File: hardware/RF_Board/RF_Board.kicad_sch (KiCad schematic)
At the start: 79 parts, among them J1 Conn_Coaxial, J2 Conn_01x07_Male, J3 Conn_Coaxial, J4 Conn_01x07_Male, J5 Conn_01x06_Female, J6 Conn_01x06_Female, J7 Conn_01x06_Female, U1 MSP430FR2355TPT, U10 QPL9096, U11 QPL9096, U12 74AHC04, U13 RFM95PW, U2 MSP430FR2355TPT, U3 CC2500, U4 HMC574, U5 HMC574, U6 YAT-5A+, U7 SKY65900-11, U8 LFCN-2750+, U9 DEA202450BT-1213C1, Y1 Crystal_GND24, Y2 Crystal, Y3 Crystal

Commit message: more work
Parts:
- added J9: LD15S33E4GX00LF, LD15S33E4GX00LF, symbol RF_Board_Symbols:LD15S33E4GX00LF
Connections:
- net +3.3V: now also J9.9
- net +5V: now also J7.3 (Pin_3), J7.4 (Pin_4), J9.15
- net CC2500_UART_RX: now also J9.7
- net CC2500_UART_TX: now also J9.8
- net GND: now also J7.5 (Pin_5), J7.6 (Pin_6), J9.12, J9.MH1, J9.MH2
- net RFM_CSN: now also J5.2 (Pin_2)
- net RFM_DIO0: now also J6.4 (Pin_4), U1.30 (P2.0/TB1.1/COMP0.O)
- net RFM_DIO1: now also J6.3 (Pin_3)
- net RFM_DIO2: now also J6.2 (Pin_2)
- net RFM_DIO3: now also J6.6 (Pin_6)
- net RFM_DIO4: now also J6.5 (Pin_5)
- net RFM_DIO5: now also J6.1 (Pin_1)
- net RFM_MISO: now also J5.5 (Pin_5)
- net RFM_MOSI: now also J5.4 (Pin_4)
- net RFM_RST: now also J5.1 (Pin_1), U1.28 (P2.2/TB1CLK)
- net RFM_SCLK: now also J5.3 (Pin_3)
- net RFM_UART_RX: now also J9.3
- net RFM_UART_TX: now also J9.4
- net RFM_3V3_OUT: now reaches U13.1 (3V3_OUT)
- net RFM_3V3_OUT: now also J5.6 (Pin_6)

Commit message: add more RF board footprints/work on layout
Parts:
- added C46: 1uF, RF_Board_Footprints:C_0603_1608Metric, symbol RF_Board_Symbols:C
- added C47: 100nF, RF_Board_Footprints:C_0603_1608Metric, symbol RF_Board_Symbols:C
- added D1, D2: D_Zener, symbol RF_Board_Symbols:D_Zener
- added D3, D4: LED, RF_Board_Footprints:LED_0603_1608Metric, symbol RF_Board_Symbols:LED
- added F1, F2: Polyfuse, symbol RF_Board_Symbols:Polyfuse
- added R10, R8, R9: 10k, symbol RF_Board_Symbols:R_US
- added R11: 10k, RF_Board_Footprints:R_0603_1608Metric, symbol RF_Board_Symbols:R_US
- added R6: 480, RF_Board_Footprints:R_0603_1608Metric, symbol RF_Board_Symbols:R_US
- added R7: 330, RF_Board_Footprints:R_0603_1608Metric, symbol RF_Board_Symbols:R_US
- C25, C36, C38, C43: footprint (none) -> RF_Board_Footprints:C_0603_1608Metric
- C37, C39, C45: footprint (none) -> RF_Board_Footprints:C_1206_3216Metric
- J1, J3: footprint (none) -> RF_Board_Footprints:SMA_Amphenol_901-144_Vertical
- U1, U2: footprint QFP50P900X900X160-48N -> RF_Board_Footprints:QFP50P900X900X160-48N
- U10, U11: footprint (none) -> RF_Board_Footprints:QPL9504TR7
- U3: footprint Package_DFN_QFN:Texas_S-PVQFN-N20_EP2.4x2.4mm -> RF_Board_Footprints:Texas_S-PVQFN-N20_EP2.4x2.4mm
- U4, U5: footprint (none) -> RF_Board_Footprints:HMC574AMS8E
- U6: footprint (none) -> RF_Board_Footprints:YAT-1A&plus_
- U7: footprint (none) -> RF_Board_Footprints:QFN-16-1EP_4x4mm_P0.65mm_EP2.5x2.5mm
- U8: footprint (none) -> RF_Board_Footprints:LFCN-2500&plus_
- U9: footprint (none) -> RF_Board_Footprints:DEA202450BT-1213C1
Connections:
- net +3.3V: now also C25.1, C46.2, C47.1, D2.1 (K), D4.1 (K), F1.2, R10.1, R8.1, R9.1; no longer J9.9
- net +5V: now also D1.1 (K), D3.1 (K), F2.2; no longer C25.1, J9.15
- net GND: now also C46.1, C47.2, D1.2 (A), D2.2 (A), R11.2, R6.2, R7.2
- net LNA_BP_A: now also U2.46 (P3.1/OA2O), R9.2
- net LNA_BP_B: now also U2.45 (P3.2/OA2-), R10.2
- net LNA_SD: now also U2.44 (P3.3/OA2+), R8.2
- net PA_EN: now also U2.38 (P3.4/SMCLK)
- net PA_VDET: now also U2.33 (P1.5/UCA0CLK/TMS/OA1O/A5)
- net RFM_DIO1: now also U1.29 (P2.1/TB1.2/COMP1.O)
- net RFM_DIO2: now also U1.28 (P2.2/TB1CLK)
- net RFM_DIO3: now also U1.27 (P2.3/TB1TRG)
- net RFM_DIO4: now also U1.11 (P2.4/COMP1.1)
- net RFM_DIO5: now also U1.10 (P2.5/COMP1.0)
- net RFM_RST: now also U1.34 (P1.4/UCA0STE/TCK/A4); no longer U1.28 (P2.2/TB1CLK)
- net SBAND_TX_RX: now also U2.37 (P3.5/OA3O), R11.1
- net CC2500_RX_EMPTY: now reaches U2.1 (P1.2/UCB0SIMO/UCB0SDA/TB0TRG/OA0-/A2/VEREF)
- net CC2500_RX_EMPTY: now also J9.5
- net CC2500_TX_OVERFLOW: now reaches U2.2 (P1.1/UCB0CLK/ACLK/OA0O/COMP0.1/A1)
- net CC2500_TX_OVERFLOW: now also J9.14
- net CC2500_RX_OVERFLOW: now reaches U2.3 (P1.0/UCB0STE/SMCLK/COMP0.0/A0/VEREF+)
- net CC2500_RX_OVERFLOW: now also J9.13
- net CC2500_TX_EMPTY: now reaches U2.48 (P1.3/UCB0SOMI/UCB0SCL/OA0+/A3)
- net CC2500_TX_EMPTY: now also J9.6
- net RFM_RX_EMPTY: now reaches U1.1 (P1.2/UCB0SIMO/UCB0SDA/TB0TRG/OA0-/A2/VEREF)
- net RFM_RX_EMPTY: now also J9.1
- net RFM_TX_OVERFLOW: now reaches U1.2 (P1.1/UCB0CLK/ACLK/OA0O/COMP0.1/A1)
- net RFM_TX_OVERFLOW: now also J9.11
- net RFM_RX_OVERFLOW: now reaches U1.3 (P1.0/UCB0STE/SMCLK/COMP0.0/A0/VEREF+)
- net RFM_RX_OVERFLOW: now also J9.10
- net RFM_TX_EMPTY: now reaches U1.48 (P1.3/UCB0SOMI/UCB0SCL/OA0+/A3)
- net RFM_TX_EMPTY: now also J9.2
- new net: D3.2 (A), R6.1
- new net: D4.2 (A), R7.1
- new net: F1.1, J9.9
- new net: F2.1, J9.15
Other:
- note added: "Power + I/O"
- note added: "S-Band"
- note added: "UHF"
- title: (none) -> R'SAT RF Board
- moved on the sheet: C1, C10, C11, C12, C13, C14, C15, C16, C17, C18, C19, C2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

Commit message: add power management to RF board + more PCB work
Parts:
- removed D1, D2: D_Zener, symbol RF_Board_Symbols:D_Zener
- removed F1, F2: Polyfuse, symbol RF_Board_Symbols:Polyfuse
- removed U12: 74AHC04, symbol RF_Board_Symbols:74AHC04
- added C48, C51: 100nF, RF_Board_Footprints:C_0603_1608Metric, symbol RF_Board_Symbols:C
- added C49, C52: 3.3nF, RF_Board_Footprints:C_0603_1608Metric, symbol RF_Board_Symbols:C
- added C50, C53: 1uF, RF_Board_Footprints:C_0805_2012Metric, symbol RF_Board_Symbols:C
- added D1, D7: D_TVS, RF_Board_Footprints:D_SMB_Handsoldering, symbol RF_Board_Symbols:D_TVS
- added D2, D8: D_Schottky, RF_Board_Footprints:D_SMB_Handsoldering, symbol Device:D_Schottky
- added D5, D6: LED, RF_Board_Footprints:LED_0603_1608Metric, symbol RF_Board_Symbols:LED
- added H1, H2, H3, H4: MountingHole_Pad, RF_Board_Footprints:MountingHole_4.3mm_M4_Pad_Via, symbol RF_Board_Symbols:MountingHole_Pad
- added Q1, Q2: 2N7002, RF_Board_Footprints:SOT-23-3, symbol RF_Board_Symbols:2N7002
- added R12, R13, R14, R15: 0, RF_Board_Footprints:R_0603_1608Metric, symbol RF_Board_Symbols:R_US
- added R16, R17: 330, RF_Board_Footprints:R_0603_1608Metric, symbol RF_Board_Symbols:R_US
- added R18: 100k, RF_Board_Footprints:R_0603_1608Metric, symbol RF_Board_Symbols:R_US
- added R19: 50k, RF_Board_Footprints:R_0603_1608Metric, symbol RF_Board_Symbols:R_US
- added R20: 3.3k, RF_Board_Footprints:R_0603_1608Metric, symbol RF_Board_Symbols:R_US
- added R21: 150k, RF_Board_Footprints:R_0603_1608Metric, symbol RF_Board_Symbols:R_US
- added R22: 39k, RF_Board_Footprints:R_0603_1608Metric, symbol RF_Board_Symbols:R_US
- added R23: 820, RF_Board_Footprints:R_0603_1608Metric, symbol RF_Board_Symbols:R_US
- added U12: 74HC04, RF_Board_Footprints:SOIC-14_3.9x8.7mm_P1.27mm, symbol RF_Board_Symbols:74HC04_ALT
- added U14, U15: TPS259573DSGR, RF_Board_Footprints:TPS259573DSGR, symbol RF_Board_Symbols:TPS259573DSGR
- C1, C16, C17, C2, C20, C21, C22, C24, C27, C28, C29, C3, C30, C31, C32, C35, C4, C5, C6, C9: footprint (none) -> RF_Board_Footprints:C_0402_1005Metric
- C10, C7: footprint (none) -> RF_Board_Footprints:C_0805_2012Metric
- C11, C12, C13, C14, C15, C19, C23, C26, C33, C34, C40, C41, C42, C44, C8, R5: footprint (none) -> RF_Board_Footprints:C_0603_1608Metric
- C18: footprint (none) -> RF_Board_Footprints:C_1206_3216Metric
- C46: footprint RF_Board_Footprints:C_0603_1608Metric -> RF_Board_Footprints:C_0805_2012Metric
- J2, J4: footprint (none) -> RF_Board_Footprints:PinHeader_1x07_P2.54mm_Vertical
- J5, J6, J7: footprint (none) -> RF_Board_Footprints:PinHeader_1x06_P2.54mm_Vertical
- J9: footprint LD15S33E4GX00LF -> RF_Board_Footprints:LD15S33E4GX00LF
- L3, L4, L5, L6: footprint (none) -> RF_Board_Footprints:L_0402_1005Metric
- R1, R10, R2, R3, R4, R8, R9: footprint (none) -> RF_Board_Footprints:R_0603_1608Metric
- Y1: footprint (none) -> RF_Board_Footprints:Crystal_SMD_3225-4Pin_3.2x2.5mm
- Y2: footprint (none) -> RF_Board_Footprints:ECS-.327-12.5-34B-TR
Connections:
- net +3.3V: now also C50.2, D2.1 (K), D5.1 (K), D6.1 (K), U12.14 (VCC), U14.5 (OUT)
- net +5V: now also C53.2, D8.1 (K), U15.5 (OUT)
- net CC2500_MOSI: now also Q1.1 (G)
- net GND: now also C48.2, C49.2, C50.1, C51.2, C52.2, C53.1, D1.2 (A2), D2.2 (A), D7.2 (A2), D8.2 (A), Q1.2 (S), Q2.2 (S), R12.2, R13.2, R14.2, R15.2, R19.2, R20.2, R22.2, R23.2, U12.7 (GND), U14.8 (GND), U14.9 (GND), U15.8 (GND), U15.9 (GND)
- net RFM_MOSI: now also Q2.1 (G)
- net SBAND_TX_RX: now also U12.1 (A1), U12.11 (A5)
- net SW1_A: now also U12.8 (Y4)
- net SW1_B: now also U12.10 (Y5), U12.9 (A4)
- net SW2_A: now also U12.6 (Y3)
- net SW2_B: now also U12.4 (Y2), U12.5 (A3)
- net 3V3_IN: now reaches J9.9
- net 3V3_IN: now also C48.1, D1.1 (A1), R18.1, U14.3 (IN), U14.4 (IN)
- net 5V0_IN: now reaches J9.15
- net 5V0_IN: now also C51.1, D7.1 (A1), R21.1, U15.3 (IN), U15.4 (IN)
- new net: D5.2 (A), R16.1
- new net: Q1.3 (D), R16.2
- new net: C49.1, U14.1 (DV_DT)
- new net: R21.2, R22.1, U15.2 (EN_UVLO)
- new net: R18.2, R19.1, U14.2 (EN_UVLO)
- new net: R20.1, U14.7 (ILM)
- new net: H2.1, R13.1
- new net: H3.1, R14.1
- new net: Q2.3 (D), R17.2
- new net: H1.1, R12.1
- new net: D6.2 (A), R17.1
- new net: C52.1, U15.1 (DV_DT)
- new net: R23.1, U15.7 (ILM)
- new net: H4.1, R15.1
- new net: U12.2 (Y1), U12.3 (A2)
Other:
- note added: "3V3 Rail: Shutdown voltage = 3.6V Shutdown current = 0.65A"
- note added: "5V0 Rail: Shutdown voltage = 5.7V Shutdown current = 2.5A"
- note added: "Consult NASA-HDBK-4001 for spacecraft grounding architecture guidelines"
- note added: "EN cutoff voltage = 1.2V"
- note added: "Rilm = 2000/(I - 0.04)"
- moved on the sheet: C25, D3, D4, J9, R11, R6, R7

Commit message: start RF Board layout
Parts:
- added R24, R25, R26, R27, R28, R29: 0, RF_Board_Footprints:R_0603_1608Metric, symbol RF_Board_Symbols:R_US
- L1, L2: value L -> 18nH; footprint (none) -> RF_Board_Footprints:L_0603_1608Metric
- Y3: footprint (none) -> RF_Board_Footprints:ECS-.327-12.5-34B-TR
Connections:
- net CC2500_MISO: now also R29.2
- net CC2500_MOSI: now also R28.2
- net CC2500_SCLK: now also R27.2
- net RFM_CSN: now also R26.1
- net RFM_DIO0: now also R24.1
- net RFM_MISO: now also R29.1
- net RFM_MOSI: now also R28.1
- net RFM_RST: now also R25.1
- net RFM_SCLK: now also R27.1
- net RFM_AUX_DIO0: now reaches U2.11 (P2.4/COMP1.1)
- net RFM_AUX_DIO0: now also R24.2
- net RFM_AUX_RST: now reaches U2.35 (P3.7/OA3+)
- net RFM_AUX_RST: now also R25.2
- net RFM_AUX_CSN: now reaches U2.36 (P3.6/OA3-)
- net RFM_AUX_CSN: now also R26.2

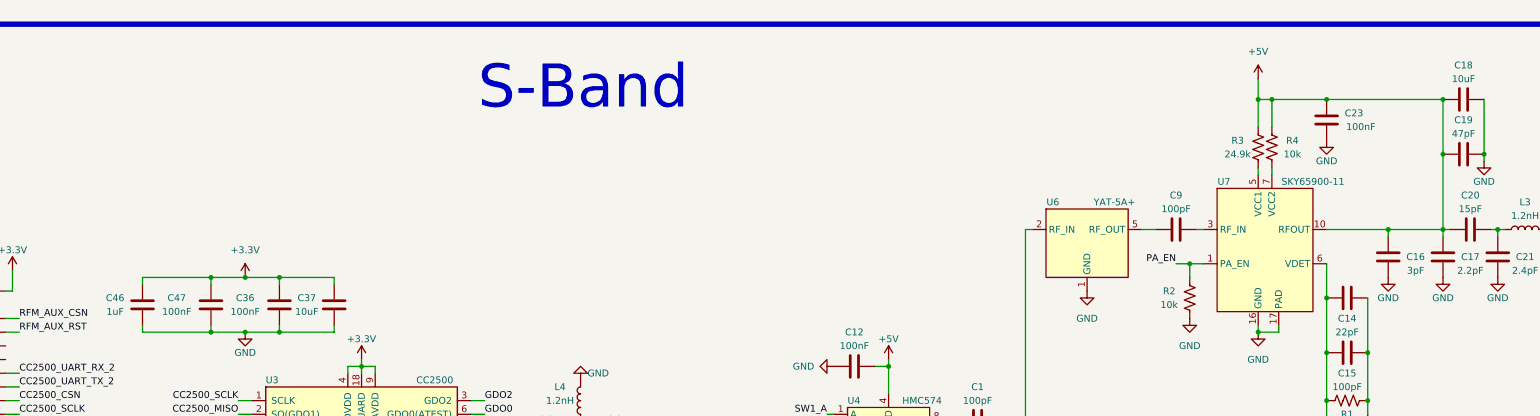
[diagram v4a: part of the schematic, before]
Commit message: RF board first draft placement
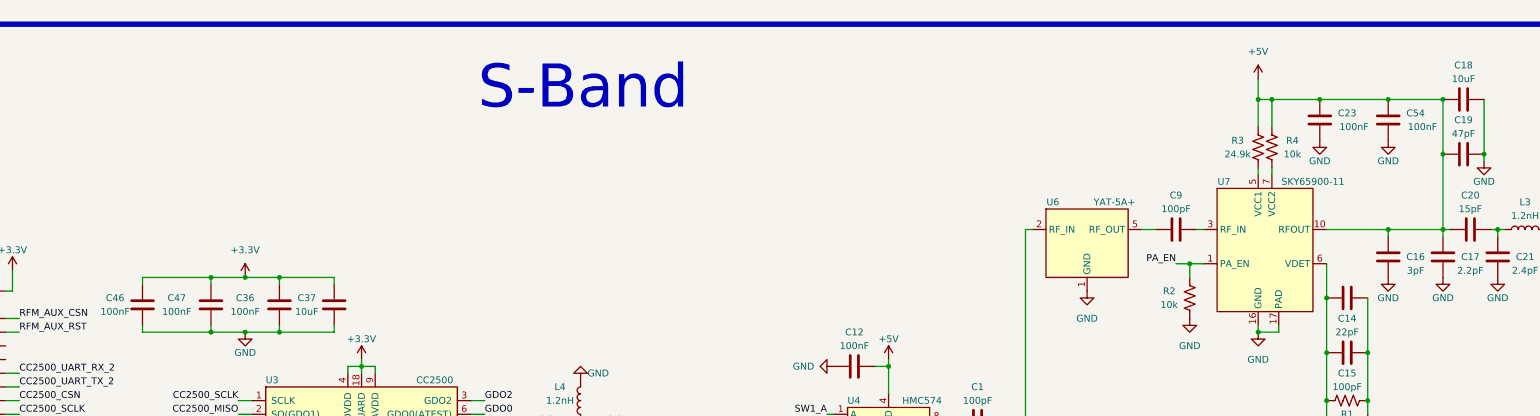
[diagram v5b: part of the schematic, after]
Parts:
- added C54: 100nF, RF_Board_Footprints:C_0603_1608Metric, symbol RF_Board_Symbols:C
- C46: value 1uF -> 100nF; footprint RF_Board_Footprints:C_0805_2012Metric -> RF_Board_Footprints:C_0603_1608Metric
- R18, R19, R20, R21, R22, R23: footprint RF_Board_Footprints:R_0603_1608Metric -> RF_Board_Footprints:R_0402_1005Metric
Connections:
- net +5V: now also C54.1
- net GND: now also C54.2
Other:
- moved on the sheet: C23
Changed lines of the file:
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@@
   (junction (at 457.2 219.71) (diameter 0) (color 0 0 0 0)
   )
+  (junction (at 447.04 195.58) (diameter 0) (color 0 0 0 0)
+  )
   (junction (at 313.69 262.89) (diameter 0) (color 0 0 0 0)
   )
@@
   (junction (at 425.45 195.58) (diameter 0) (color 0 0 0 0)
   )
-  (junction (at 435.61 195.58) (diameter 0) (color 0 0 0 0)
-  )
   (junction (at 234.95 228.6) (diameter 0) (color 0 0 0 0)
   )
   (junction (at 422.91 238.76) (diameter 0) (color 0 0 0 0)
   )
+  (junction (at 434.34 195.58) (diameter 0) (color 0 0 0 0)
+  )
   (wire (pts (xy 41.91 102.87) (xy 44.45 102.87))
     (stroke (width 0) (type default) (color 0 0 0 0))
@@
     (stroke (width 0) (type default) (color 0 0 0 0))
   )
+  (wire (pts (xy 434.34 195.58) (xy 447.04 195.58))
+    (stroke (width 0) (type default) (color 0 0 0 0))
+  )
   (wire (pts (xy 110.49 57.15) (xy 110.49 58.42))
     (stroke (width 0) (type default) (color 0 0 0 0))
@@
     (stroke (width 0) (type default) (color 0 0 0 0))
   )
+  (wire (pts (xy 447.04 195.58) (xy 457.2 195.58))
+    (stroke (width 0) (type default) (color 0 0 0 0))
+  )
   (wire (pts (xy 283.21 269.24) (xy 287.02 269.24))
     (stroke (width 0) (type default) (color 0 0 0 0))
@@
     (stroke (width 0) (type default) (color 0 0 0 0))
   )
-  (wire (pts (xy 435.61 195.58) (xy 457.2 195.58))
-    (stroke (width 0) (type default) (color 0 0 0 0))
-  )
   (wire (pts (xy 186.69 95.25) (xy 189.23 95.25))
     (stroke (width 0) (type default) (color 0 0 0 0))
@@
     (stroke (width 0) (type default) (color 0 0 0 0))
   )
-  (wire (pts (xy 425.45 195.58) (xy 435.61 195.58))
+  (wire (pts (xy 425.45 195.58) (xy 434.34 195.58))
     (stroke (width 0) (type default) (color 0 0 0 0))
   )
@@
       (effects (font (size 1.27 1.27)) (justify left))
     )
-    (property "Footprint" "RF_Board_Footprints:R_0603_1608Metric" (id 2) (at 488.696 103.124 90)
+    (property "Footprint" "RF_Board_Footprints:R_0402_1005Metric" (id 2) (at 488.696 103.124 90)
       (effects (font (size 1.27 1.27)) hide)
     )
@@
     (pin "1")
   )
+  (symbol (lib_id "power:GND") (at 447.04 203.2 0) (unit 1)
+    (in_bom yes) (on_board yes)
+    (property "Reference" "#PWR0103" (id 0) (at 447.04 209.55 0)
+      (effects (font (size 1.27 1.27)) hide)
+    )
+    (property "Value" "GND" (id 1) (at 447.04 207.01 0))
+    (property "Footprint" "" (id 2) (at 447.04 203.2 0)
+      (effects (font (size 1.27 1.27)) hide)
+    )
+    (property "Datasheet" "" (id 3) (at 447.04 203.2 0)
+      (effects (font (size 1.27 1.27)) hide)
+    )
+    (pin "1")
+  )
   (symbol (lib_id "RF_Board_Symbols:R_US") (at 487.68 59.69 0) (unit 1)
     (in_bom yes) (on_board yes) (fields_autoplaced)
@@
       (effects (font (size 1.27 1.27)) (justify left))
     )
-    (property "Footprint" "RF_Board_Footprints:R_0603_1608Metric" (id 2) (at 488.696 59.944 90)
+    (property "Footprint" "RF_Board_Footprints:R_0402_1005Metric" (id 2) (at 488.696 59.944 90)
       (effects (font (size 1.27 1.27)) hide)
     )
@@
     (pin "7")
   )
-  (symbol (lib_id "RF_Board_Symbols:C") (at 435.61 199.39 0) (unit 1)
+  (symbol (lib_id "RF_Board_Symbols:C") (at 434.34 199.39 0) (unit 1)
     (in_bom yes) (on_board yes)
-    (property "Reference" "C23" (id 0) (at 440.69 198.12 0))
-    (property "Value" "100nF" (id 1) (at 441.96 200.66 0))
-    (property "Footprint" "RF_Board_Footprints:C_0603_1608Metric" (id 2) (at 436.5752 203.2 0)
+    (property "Reference" "C23" (id 0) (at 439.42 198.12 0))
+    (property "Value" "100nF" (id 1) (at 440.69 200.66 0))
+    (property "Footprint" "RF_Board_Footprints:C_0603_1608Metric" (id 2) (at 435.3052 203.2 0)
       (effects (font (size 1.27 1.27)) hide)
     )
-    (property "Datasheet" "~" (id 3) (at 435.61 199.39 0)
+    (property "Datasheet" "~" (id 3) (at 434.34 199.39 0)
       (effects (font (size 1.27 1.27)) hide)
     )
@@
       (effects (font (size 1.27 1.27)) (justify left))
     )
-    (property "Footprint" "RF_Board_Footprints:R_0603_1608Metric" (id 2) (at 543.306 72.644 90)
+    (property "Footprint" "RF_Board_Footprints:R_0402_1005Metric" (id 2) (at 543.306 72.644 90)
       (effects (font (size 1.27 1.27)) hide)
     )
@@
     (pin "6")
   )
-  (symbol (lib_id "power:GND") (at 435.61 203.2 0) (unit 1)
+  (symbol (lib_id "power:GND") (at 434.34 203.2 0) (unit 1)
     (in_bom yes) (on_board yes)
-    (property "Reference" "#PWR025" (id 0) (at 435.61 209.55 0)
+    (property "Reference" "#PWR025" (id 0) (at 434.34 209.55 0)
       (effects (font (size 1.27 1.27)) hide)
     )
-    (property "Value" "GND" (id 1) (at 435.61 207.01 0))
-    (property "Footprint" "" (id 2) (at 435.61 203.2 0)
+    (property "Value" "GND" (id 1) (at 434.34 207.01 0))
+    (property "Footprint" "" (id 2) (at 434.34 203.2 0)
       (effects (font (size 1.27 1.27)) hide)
     )
-    (property "Datasheet" "" (id 3) (at 435.61 203.2 0)
+    (property "Datasheet" "" (id 3) (at 434.34 203.2 0)
       (effects (font (size 1.27 1.27)) hide)
     )
@@
     (pin "2")
   )
+  (symbol (lib_id "RF_Board_Symbols:C") (at 447.04 199.39 0) (unit 1)
+    (in_bom yes) (on_board yes)
+    (property "Reference" "C54" (id 0) (at 452.12 198.12 0))
+    (property "Value" "100nF" (id 1) (at 453.39 200.66 0))
+    (property "Footprint" "RF_Board_Footprints:C_0603_1608Metric" (id 2) (at 448.0052 203.2 0)
+      (effects (font (size 1.27 1.27)) hide)
+    )
+    (property "Datasheet" "~" (id 3) (at 447.04 199.39 0)
+      (effects (font (size 1.27 1.27)) hide)
+    )
+    (pin "1")
+    (pin "2")
+  )
   (symbol (lib_id "RF_Board_Symbols:R_US") (at 458.47 160.02 0) (unit 1)
     (in_bom yes) (on_board yes)
@@
     (in_bom yes) (on_board yes)
     (property "Reference" "C46" (id 0) (at 210.82 232.41 0))
-    (property "Value" "1uF" (id 1) (at 210.82 234.95 0))
-    (property "Footprint" "RF_Board_Footprints:C_0805_2012Metric" (id 2) (at 214.9348 229.87 0)
+    (property "Value" "100nF" (id 1) (at 210.82 234.95 0))
+    (property "Footprint" "RF_Board_Footprints:C_0603_1608Metric" (id 2) (at 214.9348 229.87 0)
       (effects (font (size 1.27 1.27)) hide)
     )
@@
       (effects (font (size 1.27 1.27)) (justify left))
     )
-    (property "Footprint" "RF_Board_Footprints:R_0603_1608Metric" (id 2) (at 543.306 115.824 90)
+    (property "Footprint" "RF_Board_Footprints:R_0402_1005Metric" (id 2) (at 543.306 115.824 90)
       (effects (font (size 1.27 1.27)) hide)
     )
@@
       (effects (font (size 1.27 1.27)) (justify left))
     )
-    (property "Footprint" "RF_Board_Footprints:R_0603_1608Metric" (id 2) (at 488.696 113.284 90)
+    (property "Footprint" "RF_Board_Footprints:R_0402_1005Metric" (id 2) (at 488.696 113.284 90)
       (effects (font (size 1.27 1.27)) hide)
     )
@@
       (effects (font (size 1.27 1.27)) (justify left))
     )
-    (property "Footprint" "RF_Board_Footprints:R_0603_1608Metric" (id 2) (at 488.696 70.104 90)
+    (property "Footprint" "RF_Board_Footprints:R_0402_1005Metric" (id 2) (at 488.696 70.104 90)
       (effects (font (size 1.27 1.27)) hide)
     )
@@
       (reference "#PWR0102") (unit 1) (value "GND") (footprint "")
     )
+    (path "/1eeb9d70-196f-4351-80a1-2e9f04367e28"
+      (reference "#PWR0103") (unit 1) (value "GND") (footprint "")
+    )
     (path "/e7c8c795-1b8a-4b63-81d0-1e06e03e8bd8"
       (reference "C1") (unit 1) (value "100pF") (footprint "RF_Board_Footprints:C_0402_1005Metric")
@@
     )
     (path "/ab713cb5-d701-48b5-be1c-b1690d123f28"
-      (reference "C46") (unit 1) (value "1uF") (footprint "RF_Board_Footprints:C_0805_2012Metric")
+      (reference "C46") (unit 1) (value "100nF") (footprint "RF_Board_Footprints:C_0603_1608Metric")
     )
     (path "/42dc4f5c-4e2f-4889-84aa-88e71de8c283"
@@
       (reference "C53") (unit 1) (value "1uF") (footprint "RF_Board_Footprints:C_0805_2012Metric")
     )
+    (path "/9dc24f17-fec9-47e2-99a7-43c81c0c6ccf"
+      (reference "C54") (unit 1) (value "100nF") (footprint "RF_Board_Footprints:C_0603_1608Metric")
+    )
     (path "/eece27b1-8567-4f1d-ba23-96f1695da86f"
       (reference "D1") (unit 1) (value "D_TVS") (footprint "RF_Board_Footprints:D_SMB_Handsoldering")
@@
     )
     (path "/1f240b7a-c6fc-41e6-b633-e4ea7e914632"
-      (reference "R18") (unit 1) (value "100k") (footprint "RF_Board_Footprints:R_0603_1608Metric")
+      (reference "R18") (unit 1) (value "100k") (footprint "RF_Board_Footprints:R_0402_1005Metric")
     )
     (path "/e293836a-17df-480f-a128-6664fd084507"
-      (reference "R19") (unit 1) (value "50k") (footprint "RF_Board_Footprints:R_0603_1608Metric")
+      (reference "R19") (unit 1) (value "50k") (footprint "RF_Board_Footprints:R_0402_1005Metric")
     )
     (path "/30bc8e0d-b651-43f9-8fc2-2138972f91b8"
-      (reference "R20") (unit 1) (value "3.3k") (footprint "RF_Board_Footprints:R_0603_1608Metric")
+      (reference "R20") (unit 1) (value "3.3k") (footprint "RF_Board_Footprints:R_0402_1005Metric")
     )
     (path "/0e041a24-a261-464c-a024-dbb09b51de90"
-      (reference "R21") (unit 1) (value "150k") (footprint "RF_Board_Footprints:R_0603_1608Metric")
+      (reference "R21") (unit 1) (value "150k") (footprint "RF_Board_Footprints:R_0402_1005Metric")
     )
     (path "/d1e17c80-d7fb-46ee-bbf4-b52c1ed20ad2"
-      (reference "R22") (unit 1) (value "39k") (footprint "RF_Board_Footprints:R_0603_1608Metric")
+      (reference "R22") (unit 1) (value "39k") (footprint "RF_Board_Footprints:R_0402_1005Metric")
     )
     (path "/c5d01f61-cbd8-450b-a2e8-fcb1a0fd39c2"
-      (reference "R23") (unit 1) (value "820") (footprint "RF_Board_Footprints:R_0603_1608Metric")
+      (reference "R23") (unit 1) (value "820") (footprint "RF_Board_Footprints:R_0402_1005Metric")
     )
     (path "/11f6fe50-e6ae-449a-bb49-d2c7a7c4afb4"
